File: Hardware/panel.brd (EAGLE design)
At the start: 79 x 43 mm, 86 parts, among them Q1 BC817-40LT1SMD, Q10 BC807-16LT1SMD, Q11 BC807-16LT1SMD, Q12 BC807-16LT1SMD, Q13 BC817-40LT1SMD, Q14 BC817-40LT1SMD, Q15 BC817-40LT1SMD, Q16 BC817-40LT1SMD, Q17 BC817-40LT1SMD, Q18 BC817-40LT1SMD, Q19 BC817-40LT1SMD, Q2 BC817-40LT1SMD, Q3 BC817-40LT1SMD, Q4 BC817-40LT1SMD, Q5 BC817-40LT1SMD, Q6 BC807-16LT1SMD, Q7 BC807-16LT1SMD, Q8 BC807-16LT1SMD, Q9 BC807-16LT1SMD, U1 MC7805CDT, X1 B16B-PHDSS, X2 52746-20

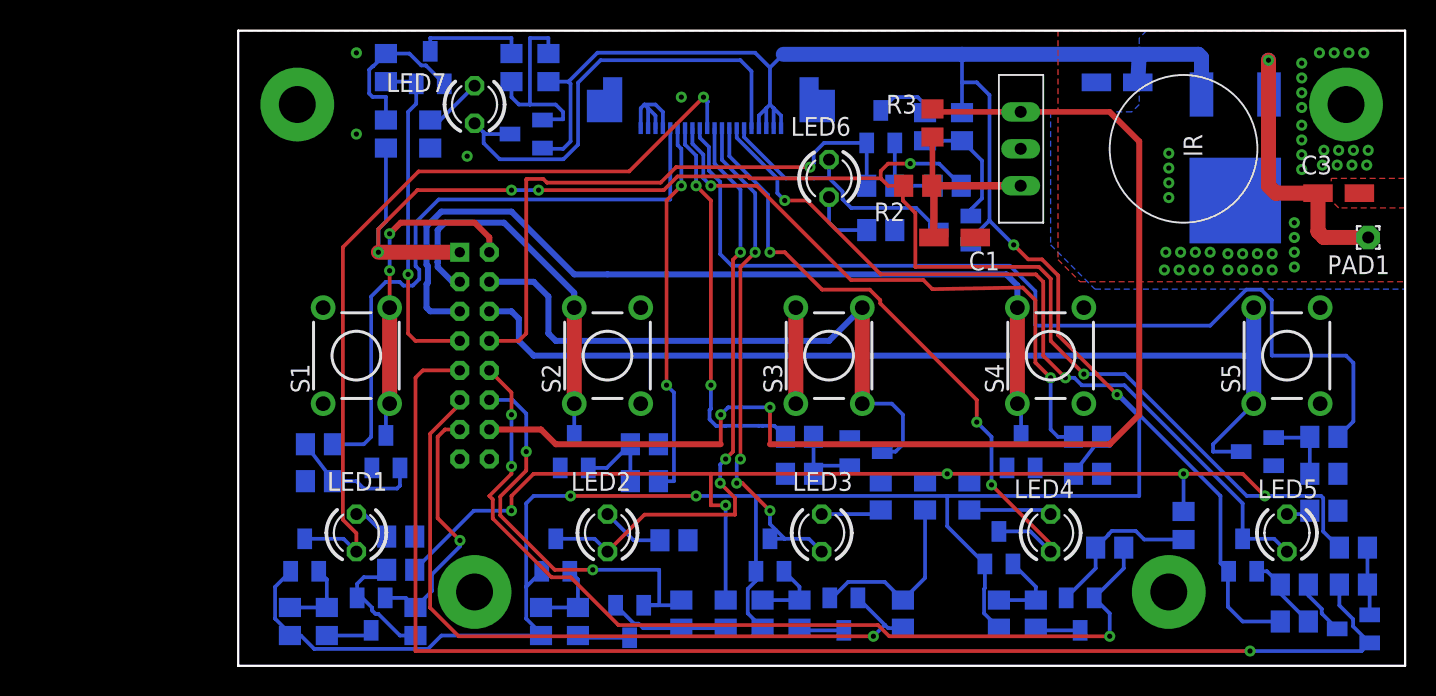
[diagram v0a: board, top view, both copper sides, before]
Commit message: убрал все, сделал тестовую схему эмуляции кнопки
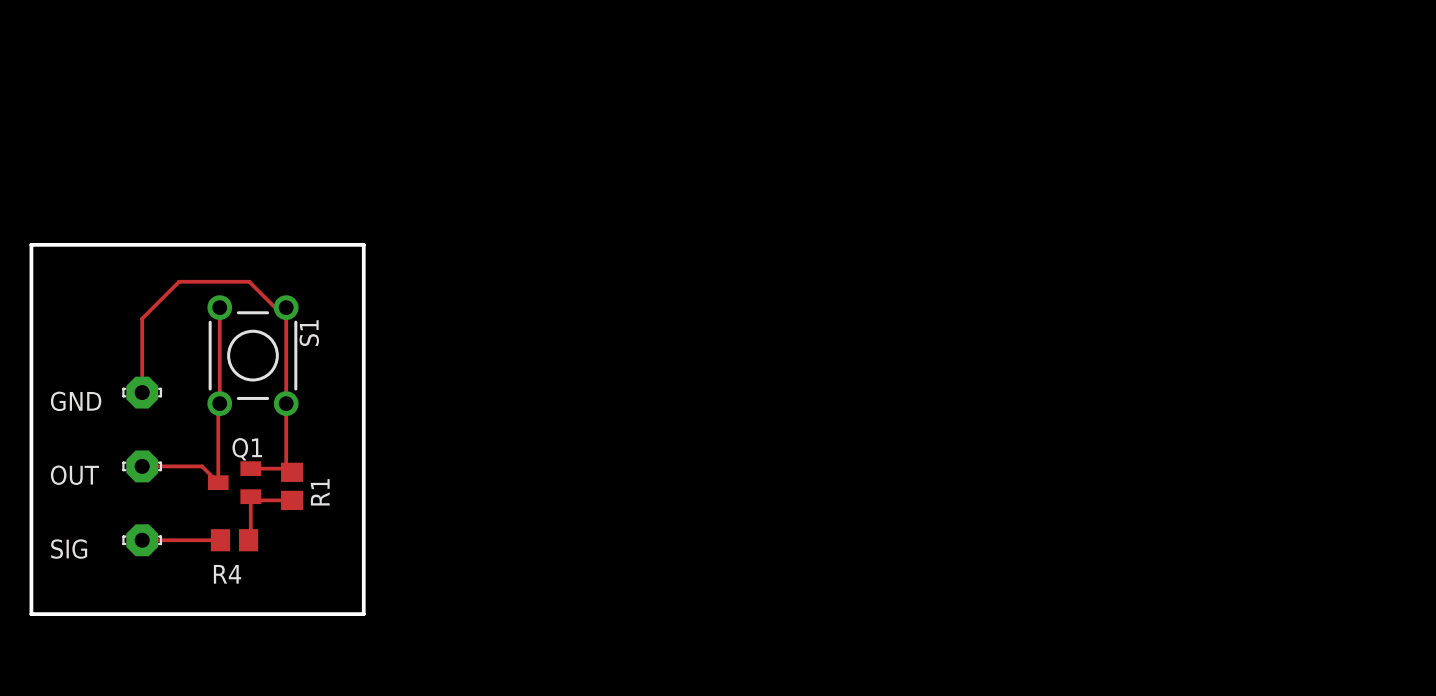
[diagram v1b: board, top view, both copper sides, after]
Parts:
- removed C1: 10uF 16v, rcl:CT3216
- removed C2: 0.33uF, rcl:CT3216
- removed C3: 0.1uF, rcl:CT3216
- removed LED1: red, led_user:LED_RED_3MM
- removed LED2, LED3, LED4, LED5, LED6, LED7: green, led_user:LED_GREEN_3MM
- removed PAD1: (no value), wirepad:1,6/0,8
- removed Q10, Q11, Q12, Q6, Q7, Q8, Q9: BC807-16LT1SMD, transistor-pnp_user:SOT23
- removed Q13, Q14, Q15, Q16, Q17, Q18, Q19, Q2, Q3, Q4, Q5: BC817-40LT1SMD, transistor-npn:SOT23-BEC
- removed R10, R11, R12, R13, R15, R16, R18, R19, R21, R22, R24, R25, R27, R28, R30, R31, R33, R34, R36, R38, R40, R42, R44, R46, R5, R6, R7, R8, R9: 4.7k, rcl:R0805
- removed R14, R17, R20, R23, R26, R29, R32: 2.2k, rcl:R0805
- removed R2: 51, rcl:R0805
- removed R3: 15k, rcl:R0805
- removed R35, R37, R39, R41, R43, R45, R47: 800, rcl:R0805
- removed S2, S3, S4, S5: 7mm, switch_user:TL1105F
- removed U$1: TSOP4838FLAT, tsop:HDRVR14W64P250_1X14_2266X508X754B
- removed U1: MC7805CDT, _hhn_78xx_79xx_NCV78xx_d2pak_dpak:DPAK-3
- removed X1: B16B-PHDSS, con-JST PHD:B16B-PHDSS
- removed X2: 52746-20, con-molex_user:52746-20
- added GND, OUT, SIG: LSP10, solpad:LSP10
- moved Q1 10.5 mm to (-1.25, 11.4), flipped to the top, turned to 90 degrees
- moved R4 8.68 mm to (-1.25, 7.50), flipped to the top
- moved S1 7.00 mm to (0.00, 20.0), turned to 180 degrees
- moved R1 1.88 mm to (2.65, 11.2), flipped to the top, turned to 270 degrees
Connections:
- removed net +24V: C2.+, Q10.2, Q11.2, Q12.2, Q6.2, Q7.2, Q8.2, Q9.2, R16.2, R18.2, R21.2, R24.2, R27.2, R30.2, R33.2, U1.1, X2.17, X2.18, X2.19, X2.20
- removed net +5V: R2.2, R35.1, R37.1, R39.1, R41.1, R43.1, R45.1, R47.1, X1.1
- removed net ADJLED: Q18.E, R44.2, X1.12
- removed net ADJLED_SIG: LED2.A, Q9.3, X2.11
- removed net DOWNLED: Q17.E, R42.2, X1.11
- removed net DOWNLED_SIG: LED3.A, Q10.3, X2.12
- removed net FFSW: Q5.C, S5.1, S5.3, X1.6
- removed net FF_SIG: R12.2, X2.9
- removed net FNSW: Q4.C, S4.1, S4.3, X1.5
- removed net FN_SIG: R10.2, X2.8
- removed net IR: R3.1, U$1.OUT, X1.14
- removed net LASERSW: Q3.C, S3.2, S3.4, X1.4
- removed net LASER_SIG: R8.2, X2.7
- removed net LVLED: Q13.E, R34.2, X1.7
- removed net LVLLED_SIG: LED7.A, Q6.3, X2.16
- removed net N$10: LED7.K, R14.2
- removed net N$11: Q14.B, R36.1, R37.2
- removed net N$12: Q7.1, R15.1, R18.1
- removed net N$13: LED6.K, R17.2
- removed net N$14: Q8.1, R19.1, R21.1
- removed net N$15: LED1.K, R20.2
- removed net N$16: Q9.1, R22.1, R24.1
- removed net N$17: LED2.K, R23.2
- removed net N$18: Q10.1, R25.1, R27.1
- removed net N$19: LED3.K, R26.2
- removed net N$2: C1.+, R2.1, R3.2, U$1.VCC
- removed net N$20: Q11.1, R28.1, R30.1
- removed net N$21: LED4.K, R29.2
- removed net N$22: Q12.1, R31.1, R33.1
- removed net N$23: LED5.K, R32.2
- removed net N$24: Q13.B, R34.1, R35.2
- removed net N$25: Q14.C, R15.2
- removed net N$26: Q15.B, R38.1, R39.2
- removed net N$27: Q15.C, R31.2
- removed net N$28: Q16.B, R40.1, R41.2
- removed net N$29: Q16.C, R28.2
- removed net N$30: Q17.B, R42.1, R43.2
- removed net N$31: Q17.C, R25.2
- removed net N$32: Q18.B, R44.1, R45.2
- removed net N$33: Q18.C, R22.2
- removed net N$34: Q19.B, R46.1, R47.2
- removed net N$35: Q19.C, R19.2
- removed net N$4: Q2.B, R5.2, R6.1
- removed net N$5: Q3.B, R7.2, R8.1
- removed net N$6: Q4.B, R10.1, R9.2
- removed net N$7: Q5.B, R11.2, R12.1
- removed net N$8: Q6.1, R13.1, R16.1
- removed net N$9: Q13.C, R13.2
- removed net PWRLED: Q19.E, R46.2, X1.13
- removed net PWRLED_SIG: LED1.A, Q8.3, X2.10
- removed net SETSW: Q2.C, S2.1, S2.3, X1.3
- removed net SET_SIG: R6.2, X2.6
- removed net UPLED: Q14.E, R36.2, X1.8
- removed net UPLED_SIG: LED6.A, Q7.3, X2.15
- removed net VOUT_SB: C3.+, PAD1.1, U1.3
- removed net XLED: Q16.E, R40.2, X1.10
- removed net XLED_SIG: LED4.A, Q11.3, X2.13
- removed net YLED: Q15.E, R38.2, X1.9
- removed net YLED_SIG: LED5.A, Q12.3, X2.14
- net GND: now also GND.MP; no longer C1.-, C2.-, C3.-, Q2.E, Q3.E, Q4.E, Q5.E, R11.1, R14.1, R17.1, R20.1, R23.1, R26.1, R29.1, R32.1, R5.1, R7.1, R9.1, S2.2, S2.4, S3.1, S3.3, S4.2, S4.4, S5.2, S5.4, U$1.GND, U1.4, X1.15, X1.16, X2.1, X2.2, X2.3, X2.4
- net PRW_SIG: now also SIG.MP; no longer X2.5
- net PWR_SW: now also OUT.MP; no longer X1.2
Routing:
- net +24V: track 222.9 -> 0.00 mm, vias 4 -> 0
- net +5V: track 179.9 -> 0.00 mm, vias 10 -> 0
- net YLED: track 91.3 -> 0.00 mm, vias 1 -> 0
- net IR: track 83.3 -> 0.00 mm, vias 2 -> 0
- net FFSW: track 66.7 -> 0.00 mm
- net FF_SIG: track 66.0 -> 0.00 mm
- net XLED: track 63.7 -> 0.00 mm, vias 3 -> 0
- net FNSW: track 60.7 -> 0.00 mm
- net PWRLED_SIG: track 55.7 -> 0.00 mm, vias 1 -> 0
- net YLED_SIG: track 54.4 -> 0.00 mm, vias 2 -> 0
- net DOWNLED: track 50.7 -> 0.00 mm, vias 1 -> 0
- net XLED_SIG: track 44.2 -> 0.00 mm, vias 3 -> 0
- net LASERSW: track 42.5 -> 0.00 mm
- net ADJLED_SIG: track 41.4 -> 0.00 mm, vias 3 -> 0
- net UPLED: track 40.7 -> 0.00 mm, vias 1 -> 0
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- removed copper zone on layer 1, net GND
- removed copper zone on layer 16, net GND
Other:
- board size 79 x 43 mm -> 22.5 x 25 mm
